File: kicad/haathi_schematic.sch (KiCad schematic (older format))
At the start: 0 parts

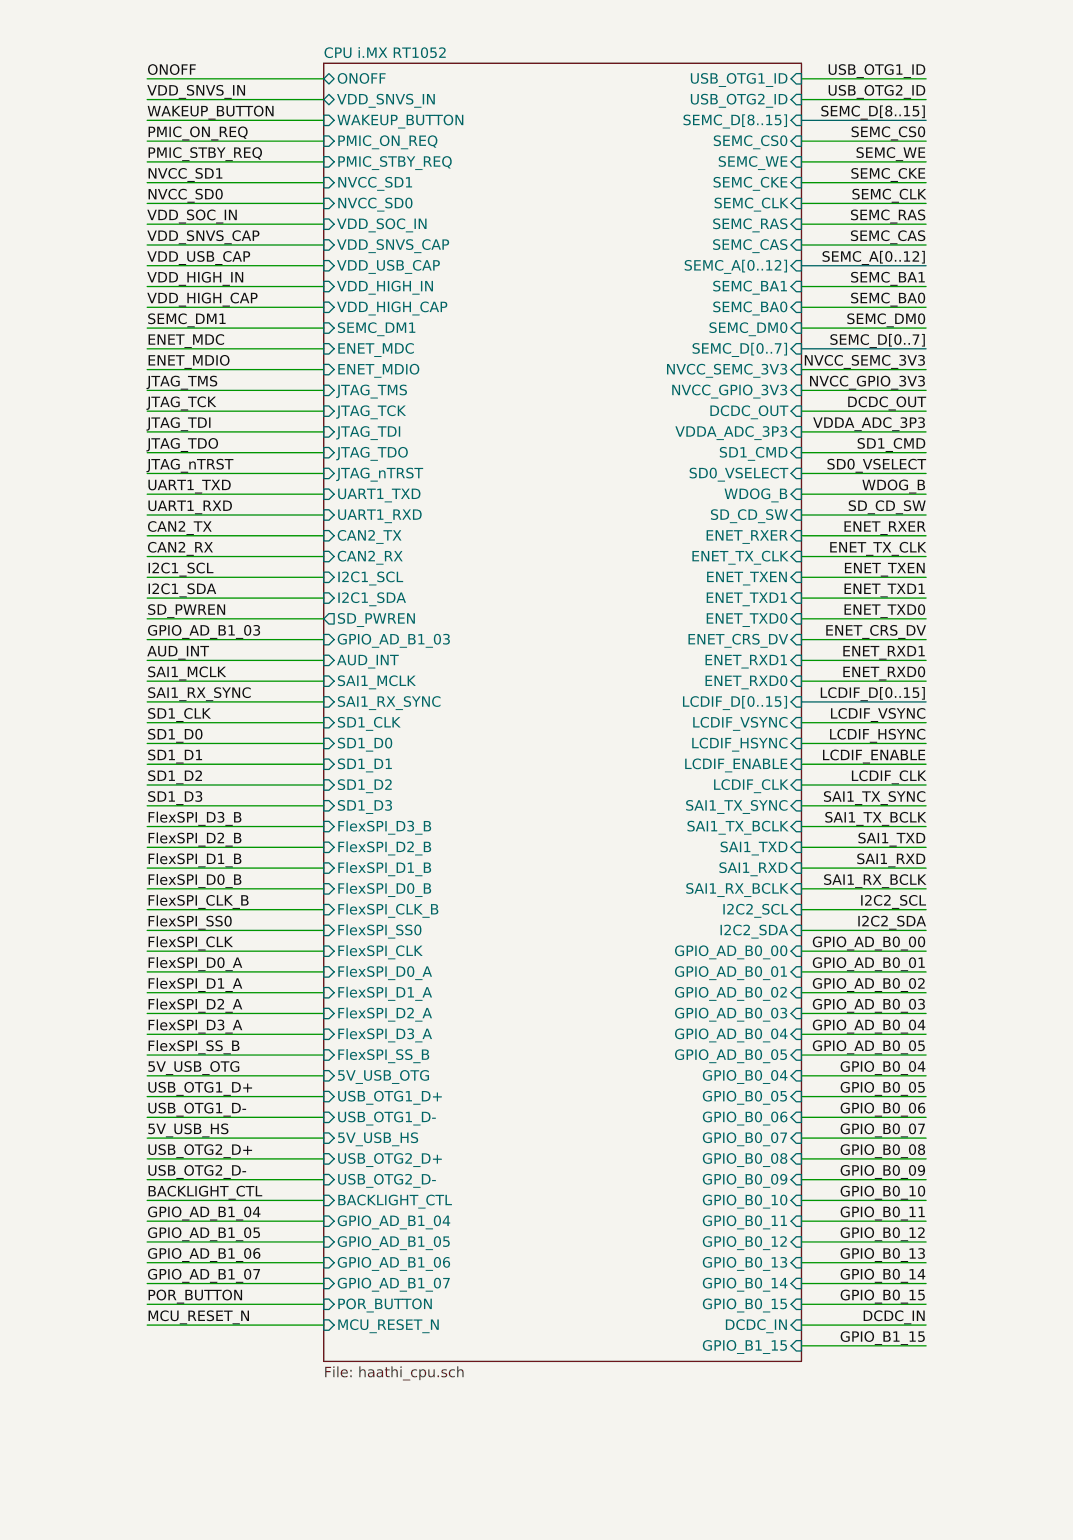
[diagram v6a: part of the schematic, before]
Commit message: Cleaned up CPU pins on top sheet
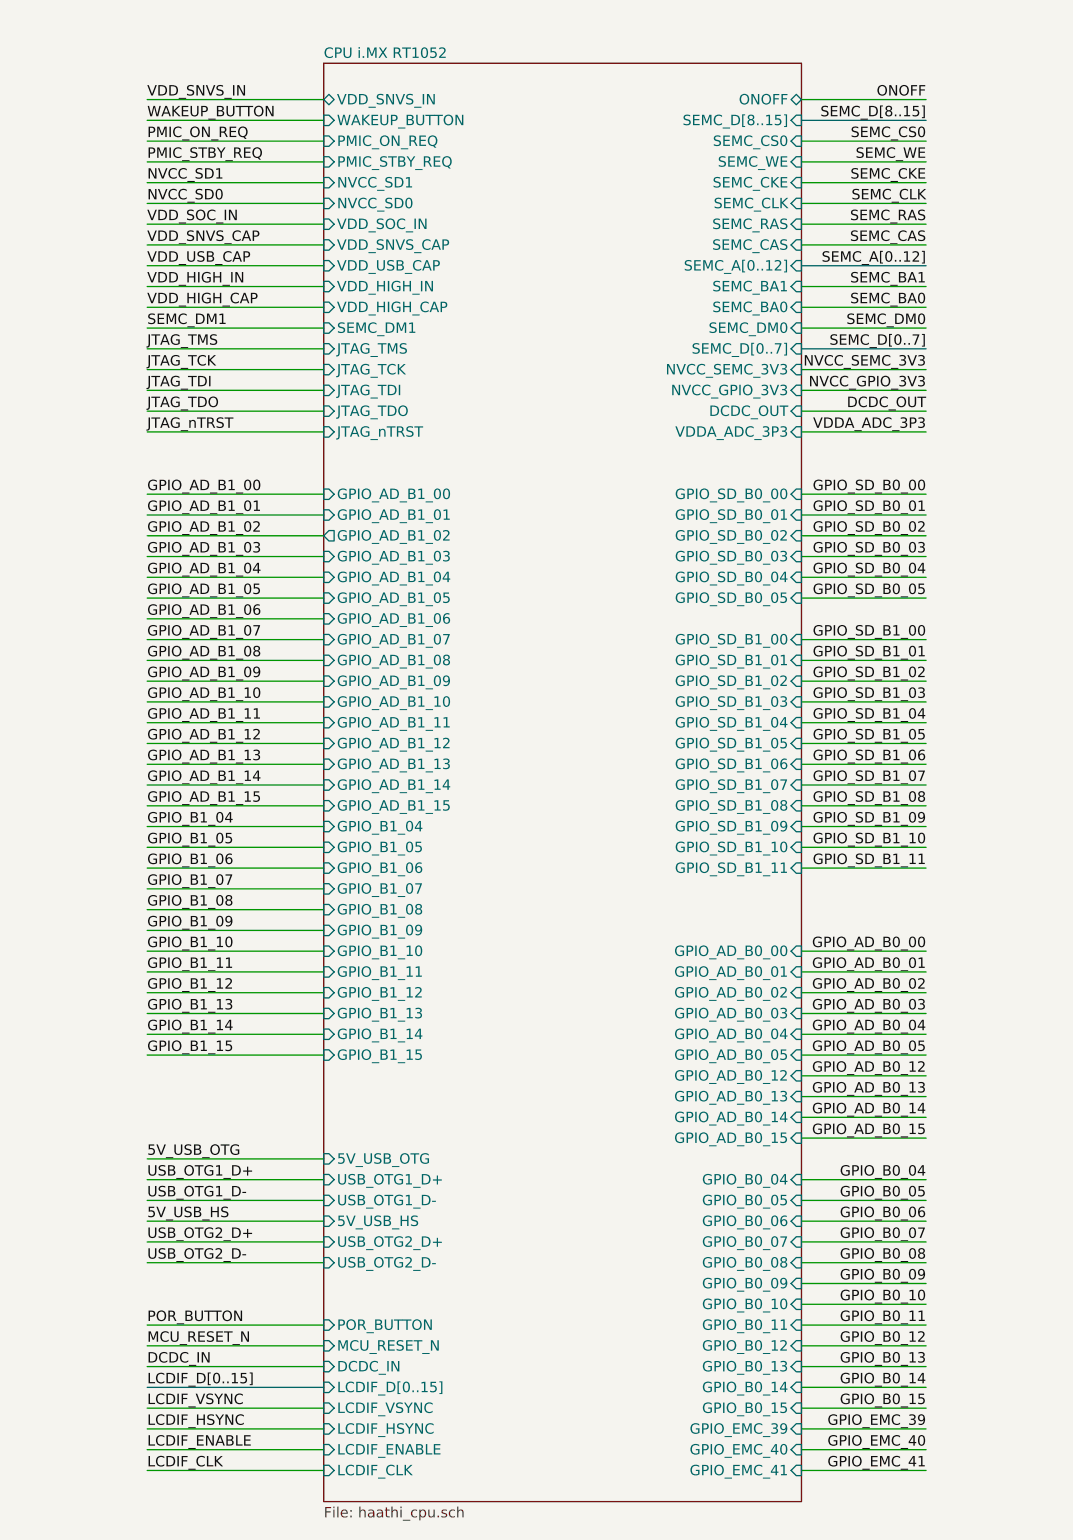
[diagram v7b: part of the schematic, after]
